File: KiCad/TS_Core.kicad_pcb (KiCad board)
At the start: 2 copper layers, 57 x 22 mm, 60 parts, among them J1 USB Serial, J2 M5StickC Hat, J3 AQM1248A, J4 TinyStick_Ext1, J5 TinyStick_Ext2, J6 Grove Connector, J7 LCD BackLight, Q1 AO3400A, SW1 Tactile, SW2 Tactile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

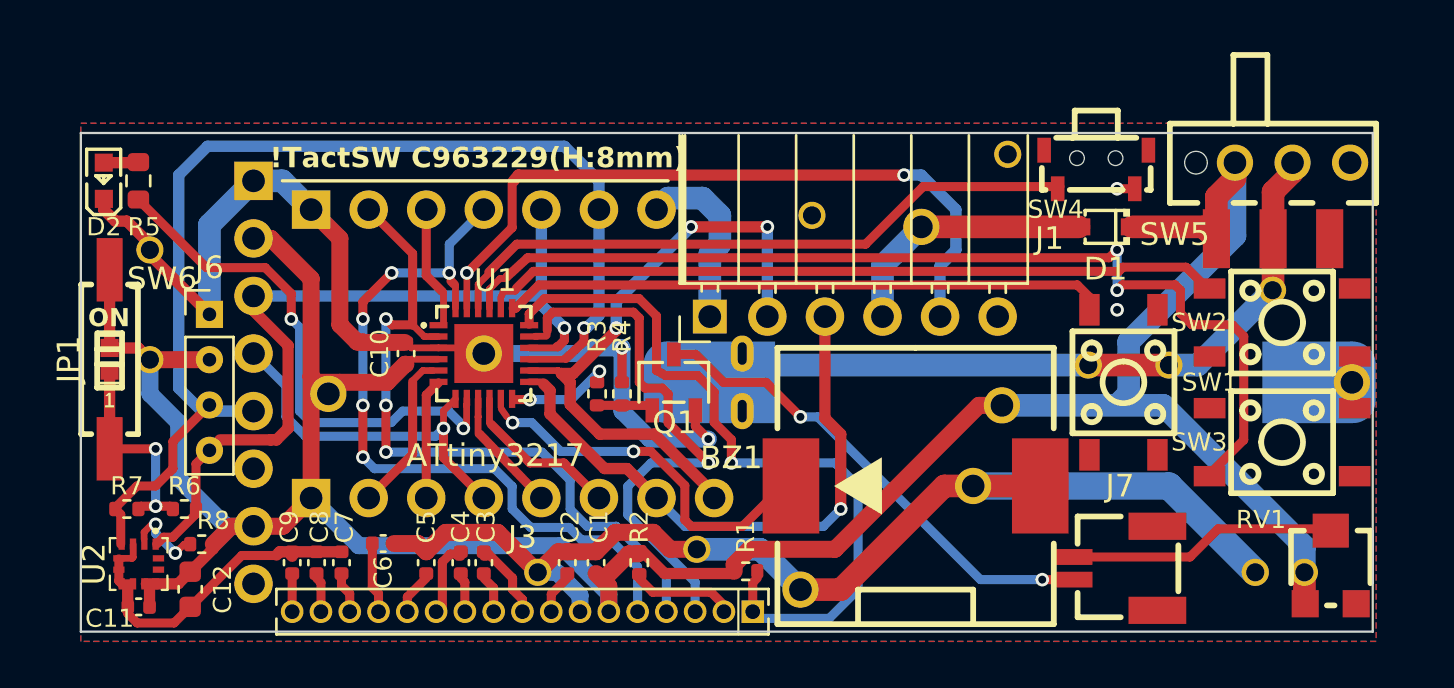
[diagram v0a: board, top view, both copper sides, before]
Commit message: update 5 buttons
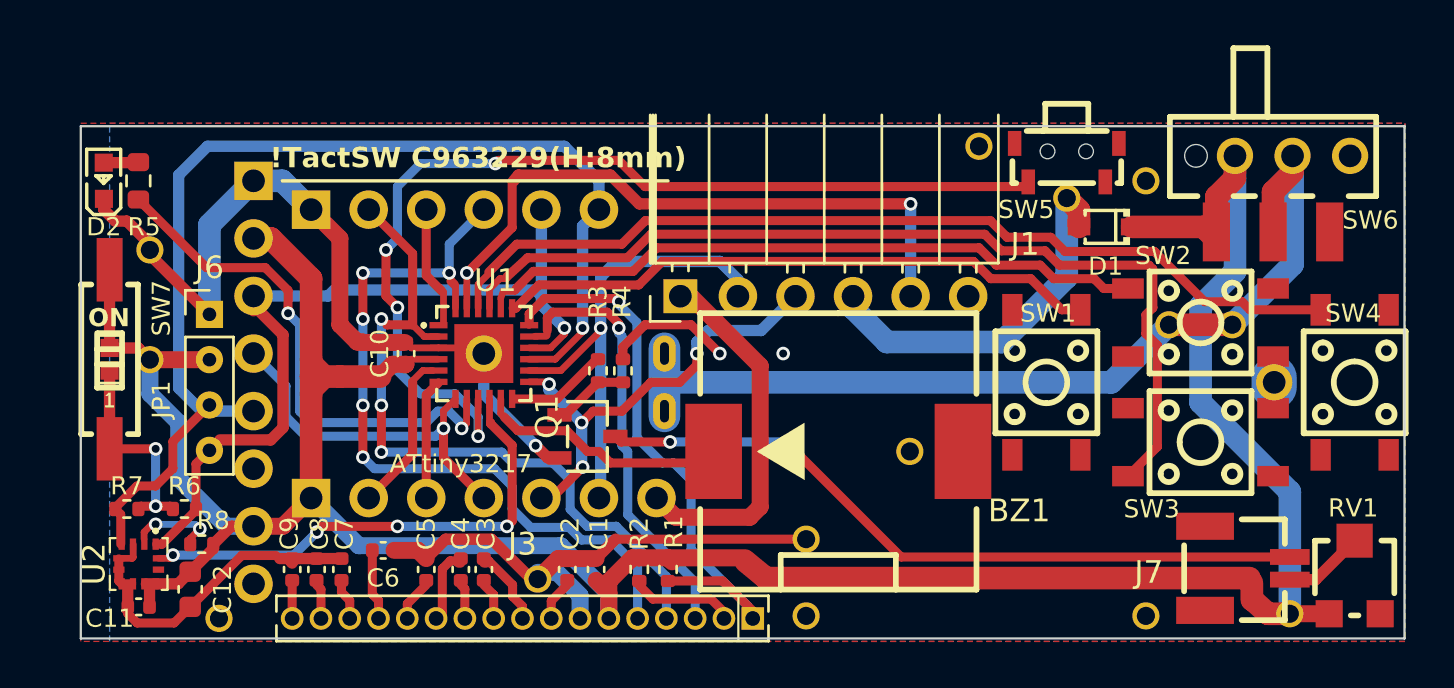
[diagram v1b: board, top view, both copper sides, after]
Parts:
- removed the ? at (57.7, 30.7)
- removed the ? at (73.4, 37.3)
- removed the ? at (69.8, 37.3)
- removed the ? at (66.3, 28.0)
- removed the ? at (78.0, 34.0)
- removed the ? at (79.2, 46.5)
- removed the ? at (66.0, 39.1)
- removed the ? at (64.8, 42.7)
- removed the ? at (36.3, 38.6)
- removed the ? at (52.6, 45.5)
- removed the ? at (62.5, 31.0)
- removed the ? at (77.2, 46.5)
- removed the ? at (57.1, 47.2)
- added ?: , , F.Cu at (31.5, 48.5)
- added ?: , , F.Cu at (72.4, 48.4)
- added ?: , , F.Cu at (69.1, 30.0)
- added ?: , , F.Cu at (76.2, 35.5)
- added ?: , , F.Cu at (73.4, 35.4)
- added ?: , , F.Cu at (57.4, 48.4)
- added ?: , , F.Cu at (65.0, 27.7)
- added ?: , , F.Cu at (72.4, 29.2)
- added ?: , , F.Cu at (62.0, 41.1)
- added ?: , , F.Cu at (57.4, 45.0)
- added ?: , , F.Cu at (78.7, 48.2)
- added SW4: Tactile, JSB01_Lib:SW-SMD_4P-L4.5-W4.5-P3.00-LS7.5, F.Cu at (81.6, 38.1)
- BT1: footprint JSB01_Lib:BAT-CR2032 -> JSB01_Lib:BAT-CR2032-2
- J4: footprint Connector_PinSocket_2.54mm:PinSocket_1x08_P2.54mm_Vertical -> Connector_PinSocket_2.54mm:PinSocket_1x07_P2.54mm_Vertical
- J5: footprint Connector_PinSocket_2.54mm:PinSocket_1x07_P2.54mm_Vertical -> Connector_PinSocket_2.54mm:PinSocket_1x06_P2.54mm_Vertical
- moved J7 5.84 mm to (76.9, 46.3), turned to -90 degrees
- moved Q1 4.50 mm to (47.8, 40.5), turned to 180 degrees
- moved BZ1 3.74 mm to (58.8, 41.1)
- moved SW2 3.60 mm to (74.8, 35.5)
- moved SW3 3.60 mm to (74.8, 40.7)
- moved BT1 3.43 mm to (64.6, 38.1)
- moved R1 3.43 mm to (51.3, 46.4), turned to -90 degrees
- moved SW1 3.40 mm to (68.0, 38.1), turned to -90 degrees
- moved J1 1.58 mm to (58.2, 34.3)
- moved SW5 1.33 mm to (68.9, 28.4)
- moved RV1 1.14 mm to (81.6, 46.7)
- moved R3 1.02 mm to (48.2, 37.6)
- moved R4 1.02 mm to (49.3, 37.6)
- moved C1 0.30 mm to (48.1, 46.4)
- moved C2 0.30 mm to (46.9, 46.4)
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- renumbered SW4 to SW5, SW5 to SW6, SW6 to SW7
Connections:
- BT1 pad : (no net) -> Net-(BT1-+)
- J4 pad 5: PB7 -> RXD
- J4 pad 6: PB6 -> TXD
- J4 pad 7: RXD -> +5V
- SW5 pad 1: SW4 -> SW5
- U1 pad 9: PB7 -> SW5
- U2 pad 12: unconnected-(U2-INT2-Pad12) -> PB6
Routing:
- net SW5: track 0.00 -> 44.4 mm, vias 0 -> 4
- net GND: track 111.6 -> 79.3 mm, vias 4 -> 3
- net PB6: track 7.25 -> 21.6 mm, vias 0 -> 4
- net SW4: track 28.5 -> 41.0 mm
- net Net-(J7-LCD_BL_K): track 21.7 -> 32.0 mm
- net +5V: track 7.97 -> 16.2 mm
- net Net-(J7-LCD_BL_A): track 11.7 -> 3.57 mm
- net LCD_CS: track 33.2 -> 25.8 mm
- net TXD: track 28.6 -> 21.6 mm, vias 3 -> 1
- net RXD: track 26.8 -> 20.3 mm, vias 1 -> 4
- net Buz: track 16.2 -> 10.4 mm, vias 2 -> 0
- net LCD_RS: track 24.5 -> 18.9 mm
- net +3V3: track 125.8 -> 131.3 mm
- net PB7: track 5.47 -> 0.00 mm
- net Net-(D1-A): track 11.7 -> 16.7 mm
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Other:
- board size 57 x 22 mm -> 58.4 x 22.6 mm
- board text added: "TinyStick Rev 0.5"
- board text removed: "TinyStick Rev 0.4"
